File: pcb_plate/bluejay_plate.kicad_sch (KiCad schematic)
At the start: 33 parts

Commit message: Fine tune pcbs
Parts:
- H4: symbol Mechanical:MountingHole -> Mechanical:MountingHole_Pad; now in the parts list
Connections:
- net GND: now also H4.1
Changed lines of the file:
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@@
     (title "BlueJay Plate")
+  )
+  (junction (at 208.28 165.1) (diameter 0) (color 0 0 0 0)
+  )
+  (wire (pts (xy 208.28 165.1) (xy 226.06 165.1))
+    (stroke (width 0) (type default) (color 0 0 0 0))
   )
   (symbol (lib_id "BlueJaySymbolLibrary:Switch_SW_Push") (at 218.44 119.38 90) (unit 1)
@@
     (pin "2")
   )
-  (symbol (lib_id "Mechanical:MountingHole") (at 226.06 162.56 0) (unit 1)
-    (in_bom no) (on_board yes) (fields_autoplaced)
+  (symbol (lib_id "Mechanical:MountingHole_Pad") (at 226.06 162.56 0) (unit 1)
+    (in_bom yes) (on_board yes) (fields_autoplaced)
     (property "Reference" "H4" (id 0) (at 228.6 161.2899 0)
       (effects (font (size 1.27 1.27)) (justify left))
@@
       (effects (font (size 1.27 1.27)) hide)
     )
+    (pin "1")
   )
   (symbol (lib_id "BlueJaySymbolLibrary:Switch_SW_Push") (at 218.44 133.35 90) (unit 1)

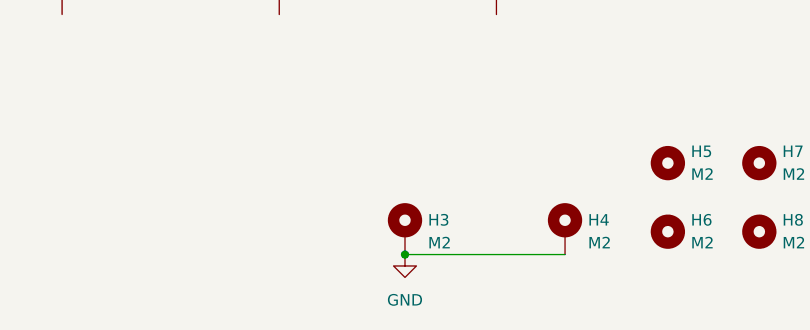
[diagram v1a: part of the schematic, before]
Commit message: Update schematics in preparation for review
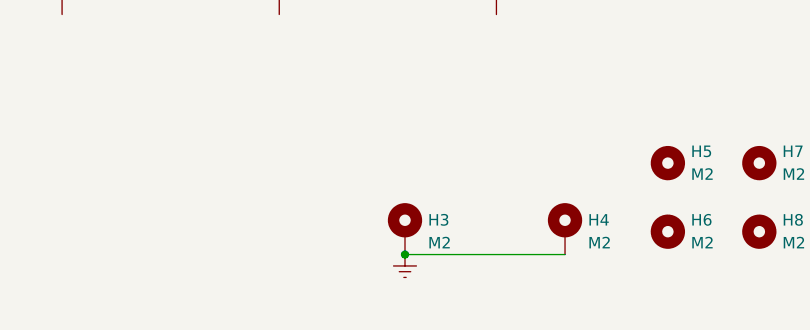
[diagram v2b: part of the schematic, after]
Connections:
- net GND renamed Earth
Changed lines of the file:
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@@
   (title_block
     (title "BlueJay Plate")
+    (rev "1.0")
   )
   (junction (at 208.28 165.1) (diameter 0) (color 0 0 0 0)
@@
     (pin "2")
   )
-  (symbol (lib_id "power:GND") (at 208.28 165.1 0) (unit 1)
+  (symbol (lib_id "power:Earth") (at 208.28 165.1 0) (unit 1)
     (in_bom yes) (on_board yes) (fields_autoplaced)
     (property "Reference" "#PWR0115" (id 0) (at 208.28 171.45 0)
       (effects (font (size 1.27 1.27)) hide)
     )
-    (property "Value" "GND" (id 1) (at 208.28 170.18 0))
+    (property "Value" "Earth" (id 1) (at 208.28 168.91 0)
+      (effects (font (size 1.27 1.27)) hide)
+    )
     (property "Footprint" "" (id 2) (at 208.28 165.1 0)
       (effects (font (size 1.27 1.27)) hide)
     )
-    (property "Datasheet" "" (id 3) (at 208.28 165.1 0)
+    (property "Datasheet" "~" (id 3) (at 208.28 165.1 0)
       (effects (font (size 1.27 1.27)) hide)
     )
@@
   (symbol_instances
     (path "/aa799aa4-0b77-4e69-bd3a-b95b04823f1a"
-      (reference "#PWR0115") (unit 1) (value "GND") (footprint "")
+      (reference "#PWR0115") (unit 1) (value "Earth") (footprint "")
     )
     (path "/552b5d1f-a593-40c3-a973-202071f3c188"

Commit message: Fine tuning of schematics and pcbs in prep for review
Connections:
- net Earth renamed GND
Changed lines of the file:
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@@
+    (stroke (width 0) (type default) (color 0 0 0 0))
+  )
+  (wire (pts (xy 208.28 166.37) (xy 208.28 165.1))
     (stroke (width 0) (type default) (color 0 0 0 0))
   )
@@
     (pin "2")
   )
-  (symbol (lib_id "power:Earth") (at 208.28 165.1 0) (unit 1)
-    (in_bom yes) (on_board yes) (fields_autoplaced)
-    (property "Reference" "#PWR0115" (id 0) (at 208.28 171.45 0)
-      (effects (font (size 1.27 1.27)) hide)
-    )
-    (property "Value" "Earth" (id 1) (at 208.28 168.91 0)
-      (effects (font (size 1.27 1.27)) hide)
-    )
-    (property "Footprint" "" (id 2) (at 208.28 165.1 0)
-      (effects (font (size 1.27 1.27)) hide)
-    )
-    (property "Datasheet" "~" (id 3) (at 208.28 165.1 0)
+  (symbol (lib_id "power:GND") (at 208.28 166.37 0) (unit 1)
+    (in_bom yes) (on_board yes) (fields_autoplaced)
+    (property "Reference" "#PWR0115" (id 0) (at 208.28 172.72 0)
+      (effects (font (size 1.27 1.27)) hide)
+    )
+    (property "Value" "GND" (id 1) (at 208.28 170.18 0))
+    (property "Footprint" "" (id 2) (at 208.28 166.37 0)
+      (effects (font (size 1.27 1.27)) hide)
+    )
+    (property "Datasheet" "~" (id 3) (at 208.28 166.37 0)
       (effects (font (size 1.27 1.27)) hide)
     )
@@
   (symbol_instances
     (path "/aa799aa4-0b77-4e69-bd3a-b95b04823f1a"
-      (reference "#PWR0115") (unit 1) (value "Earth") (footprint "")
+      (reference "#PWR0115") (unit 1) (value "GND") (footprint "")
     )
     (path "/552b5d1f-a593-40c3-a973-202071f3c188"

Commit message: Update placement of some components and size of drill holes
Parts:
- H3, H4, H5, H6, H7, H8: footprint MountingHole:MountingHole_2.2mm_M2_Pad -> BlueJay footprints:Drill hole
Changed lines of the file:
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@@
       (effects (font (size 1.27 1.27)) (justify left))
     )
-    (property "Footprint" "MountingHole:MountingHole_2.2mm_M2_Pad" (id 2) (at 208.28 162.56 0)
+    (property "Footprint" "BlueJay footprints:Drill hole" (id 2) (at 208.28 162.56 0)
       (effects (font (size 1.27 1.27)) hide)
     )
@@
       (effects (font (size 1.27 1.27)) (justify left))
     )
-    (property "Footprint" "MountingHole:MountingHole_2.2mm_M2_Pad" (id 2) (at 237.49 162.56 0)
+    (property "Footprint" "BlueJay footprints:Drill hole" (id 2) (at 237.49 162.56 0)
       (effects (font (size 1.27 1.27)) hide)
     )
@@
       (effects (font (size 1.27 1.27)) (justify left))
     )
-    (property "Footprint" "MountingHole:MountingHole_2.2mm_M2_Pad" (id 2) (at 237.49 154.94 0)
+    (property "Footprint" "BlueJay footprints:Drill hole" (id 2) (at 237.49 154.94 0)
       (effects (font (size 1.27 1.27)) hide)
     )
@@
       (effects (font (size 1.27 1.27)) (justify left))
     )
-    (property "Footprint" "MountingHole:MountingHole_2.2mm_M2_Pad" (id 2) (at 247.65 154.94 0)
+    (property "Footprint" "BlueJay footprints:Drill hole" (id 2) (at 247.65 154.94 0)
       (effects (font (size 1.27 1.27)) hide)
     )
@@
       (effects (font (size 1.27 1.27)) (justify left))
     )
-    (property "Footprint" "MountingHole:MountingHole_2.2mm_M2_Pad" (id 2) (at 247.65 162.56 0)
+    (property "Footprint" "BlueJay footprints:Drill hole" (id 2) (at 247.65 162.56 0)
       (effects (font (size 1.27 1.27)) hide)
     )
@@
       (effects (font (size 1.27 1.27)) (justify left))
     )
-    (property "Footprint" "MountingHole:MountingHole_2.2mm_M2_Pad" (id 2) (at 226.06 162.56 0)
+    (property "Footprint" "BlueJay footprints:Drill hole" (id 2) (at 226.06 162.56 0)
       (effects (font (size 1.27 1.27)) hide)
     )
@@
     )
     (path "/552b5d1f-a593-40c3-a973-202071f3c188"
-      (reference "H3") (unit 1) (value "M2") (footprint "MountingHole:MountingHole_2.2mm_M2_Pad")
+      (reference "H3") (unit 1) (value "M2") (footprint "BlueJay footprints:Drill hole")
     )
     (path "/c9aec2e8-4e37-4baa-9790-b0363dbc3f18"
-      (reference "H4") (unit 1) (value "M2") (footprint "MountingHole:MountingHole_2.2mm_M2_Pad")
+      (reference "H4") (unit 1) (value "M2") (footprint "BlueJay footprints:Drill hole")
     )
     (path "/6dcbd964-e53a-42c2-bb2f-1604534332d7"
-      (reference "H5") (unit 1) (value "M2") (footprint "MountingHole:MountingHole_2.2mm_M2_Pad")
+      (reference "H5") (unit 1) (value "M2") (footprint "BlueJay footprints:Drill hole")
     )
     (path "/6133af06-e5a9-4dea-9d88-3fa37672e076"
-      (reference "H6") (unit 1) (value "M2") (footprint "MountingHole:MountingHole_2.2mm_M2_Pad")
+      (reference "H6") (unit 1) (value "M2") (footprint "BlueJay footprints:Drill hole")
     )
     (path "/8ff55002-cb98-4e23-b57e-209cc7ec712a"
-      (reference "H7") (unit 1) (value "M2") (footprint "MountingHole:MountingHole_2.2mm_M2_Pad")
+      (reference "H7") (unit 1) (value "M2") (footprint "BlueJay footprints:Drill hole")
     )
     (path "/a73aae4f-b04b-4d16-8b11-ca3d57da8772"
-      (reference "H8") (unit 1) (value "M2") (footprint "MountingHole:MountingHole_2.2mm_M2_Pad")
+      (reference "H8") (unit 1) (value "M2") (footprint "BlueJay footprints:Drill hole")
     )
     (path "/b8ba3aba-b327-4c38-851e-02054b6b4e1d"
